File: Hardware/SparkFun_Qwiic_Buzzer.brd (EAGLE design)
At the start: 25.4 x 25.4 mm, 65 parts, among them J2 QWIIC_RA, J3 QWIIC_RA, Q3 200mA/40V, U4 ATTINY84-ARDUINO

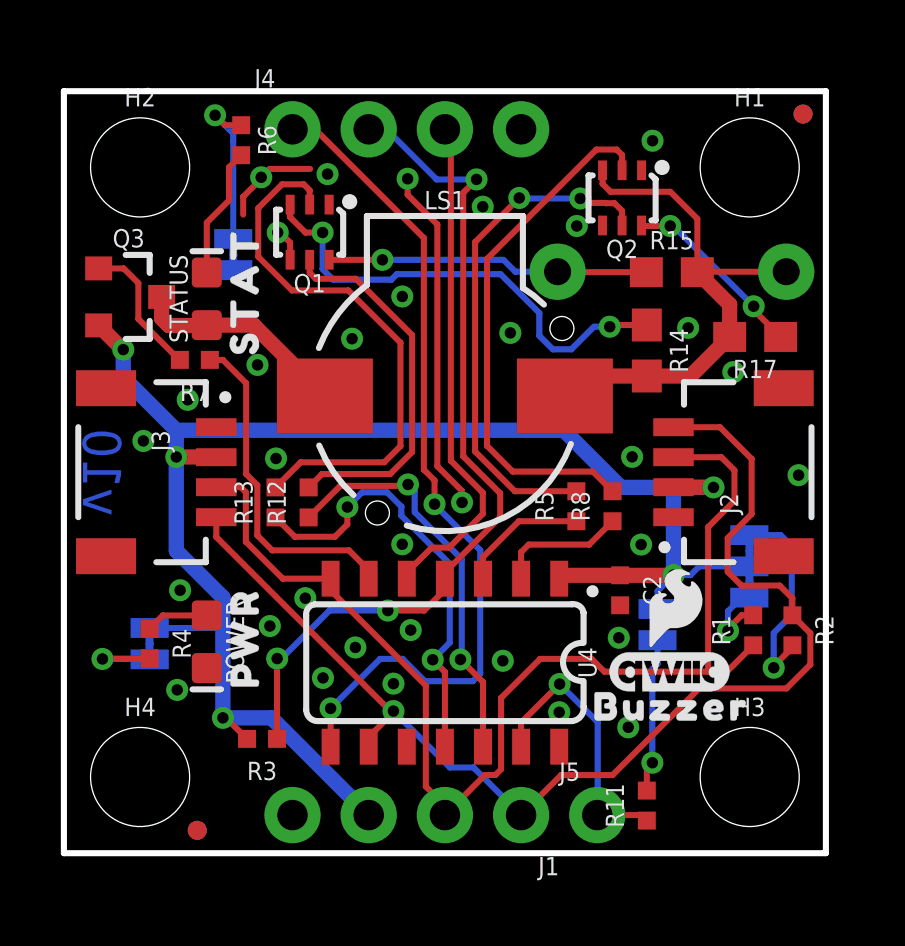
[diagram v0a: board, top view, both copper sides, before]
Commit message: group review pre-meeting
-add flyback diode
-add tPlace lines to divide tightly packed passives
-add 10uF cap on 3V3 rail
-corrected name on I2C Jumper
-Added JP1 to allow user to easily remove R15 resistor when using USER PTH resistor for volume control
-fixes some acid traps on poci and rst headers
-increased trace from USER resistor to BJT.
-trigger net renames to have active low in the name
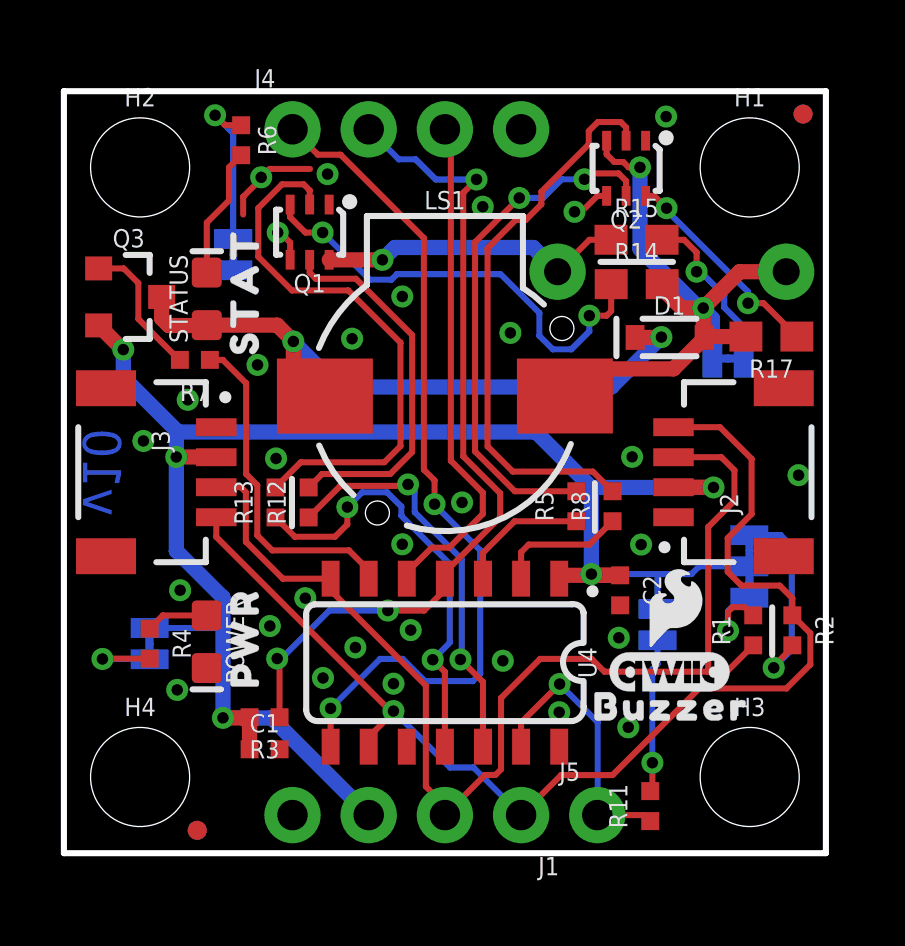
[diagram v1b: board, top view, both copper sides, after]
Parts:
- added C1: 10uF, SparkFun-Capacitors:0402-TIGHT
- added D1: 0.5A/40V/420mV, SparkFun-DiscreteSemi:SOD-323
- added JP1: (no value), SparkFun-Jumpers:SMT-JUMPER_2_NC_TRACE_SILK
- added U$5: (no value), output:#PWR_LED#13
- U$6: device output:#PWR#4 -> output:#JP1#14
- moved U$6 17.7 mm to (19.5, 16.3), turned to 0 degrees
- moved R14 2.24 mm to (19.1, 19.0), turned to 0 degrees
- moved R15 1.60 mm to (19.1, 20.4)
- moved Q2 0.99 mm to (18.7, 22.8)
- moved R3 0.73 mm to (6.69, 4.53)
- moved R17 0.54 mm to (23.6, 17.2)
- moved R11 0.12 mm to (19.5, 1.57)
- renumbered JP3 to I2C, PWR to PWR_LED
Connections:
- net TRIGGER renamed !TRIGGER!
- new net N$16: JP1.1, R15.2
- net 3.3V: now also C1.1
- net GND: now also C1.2
- net N$4: now also D1.A, JP1.2; no longer R15.2
- net N$6: now also D1.C
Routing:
- net N$6: track 7.24 -> 22.2 mm, vias 0 -> 2
- net GND: track 15.9 -> 5.67 mm, vias 33 -> 30
- net N$16: track 0.00 -> 5.59 mm, vias 0 -> 1
- net N$4: track 17.8 -> 22.1 mm, vias 0 -> 2
- net 3.3V: track 56.7 -> 59.2 mm
- net N$12: track 17.6 -> 18.8 mm
- net N$13: track 6.25 -> 7.25 mm
- net !RST: track 28.6 -> 28.0 mm
- net SDA_PU1: track 2.65 -> 3.21 mm
- net N$14: track 15.8 -> 15.3 mm

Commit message: reduced size of qwiic logo and buzzer test on bottom silk
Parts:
- removed U$14: (no value), output:BUZZER0
- added U$22: (no value), output:BUZZER14
- U$16: device SparkFun-Aesthetics:QWIIC_7MM -> SparkFun-Aesthetics:QWIIC_5MM
- moved U$16 0.49 mm to (13.1, 10.3)
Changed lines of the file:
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@@
 <drawing>
 <settings>
-<setting alwaysvectorfont="yes"/>
+<setting alwaysvectorfont="no"/>
 <setting keepoldvectorfont="yes"/>
 <setting verticaltext="up"/>
@@
 <grid distance="0.05" unitdist="inch" unit="inch" style="lines" multiple="1" display="yes" altdistance="0.0001" altunitdist="inch" altunit="inch"/>
 <layers>
-<layer number="1" name="Top" color="4" fill="1" visible="yes" active="yes"/>
-<layer number="16" name="Bottom" color="1" fill="1" visible="yes" active="yes"/>
+<layer number="1" name="Top" color="4" fill="1" visible="no" active="yes"/>
+<layer number="16" name="Bottom" color="1" fill="1" visible="no" active="yes"/>
 <layer number="17" name="Pads" color="2" fill="1" visible="yes" active="yes"/>
 <layer number="18" name="Vias" color="2" fill="1" visible="yes" active="yes"/>
-<layer number="19" name="Unrouted" color="6" fill="1" visible="yes" active="yes"/>
-<layer number="20" name="Dimension" color="24" fill="1" visible="yes" active="yes"/>
-<layer number="21" name="tPlace" color="16" fill="1" visible="yes" active="yes"/>
+<layer number="19" name="Unrouted" color="6" fill="1" visible="no" active="yes"/>
+<layer number="20" name="Dimension" color="24" fill="1" visible="no" active="yes"/>
+<layer number="21" name="tPlace" color="16" fill="1" visible="no" active="yes"/>
 <layer number="22" name="bPlace" color="14" fill="1" visible="yes" active="yes"/>
-<layer number="23" name="tOrigins" color="15" fill="1" visible="yes" active="yes"/>
+<layer number="23" name="tOrigins" color="15" fill="1" visible="no" active="yes"/>
 <layer number="24" name="bOrigins" color="15" fill="1" visible="yes" active="yes"/>
 <layer number="25" name="tNames" color="7" fill="1" visible="no" active="yes"/>
@@
 <layer number="37" name="tTest" color="7" fill="1" visible="no" active="yes"/>
 <layer number="38" name="bTest" color="7" fill="1" visible="no" active="yes"/>
-<layer number="39" name="tKeepout" color="4" fill="11" visible="yes" active="yes"/>
+<layer number="39" name="tKeepout" color="4" fill="11" visible="no" active="yes"/>
 <layer number="40" name="bKeepout" color="1" fill="11" visible="no" active="yes"/>
 <layer number="41" name="tRestrict" color="4" fill="10" visible="no" active="yes"/>
@@
 <layer number="43" name="vRestrict" color="2" fill="10" visible="no" active="yes"/>
 <layer number="44" name="Drills" color="7" fill="1" visible="no" active="yes"/>
-<layer number="45" name="Holes" color="7" fill="1" visible="yes" active="yes"/>
+<layer number="45" name="Holes" color="7" fill="1" visible="no" active="yes"/>
 <layer number="46" name="Milling" color="3" fill="1" visible="no" active="yes"/>
 <layer number="47" name="Measures" color="7" fill="1" visible="no" active="yes"/>
 <layer number="48" name="Document" color="7" fill="1" visible="no" active="yes"/>
-<layer number="49" name="Reference" color="7" fill="1" visible="yes" active="yes"/>
+<layer number="49" name="Reference" color="7" fill="1" visible="no" active="yes"/>
 <layer number="50" name="dxf" color="7" fill="1" visible="no" active="yes"/>
-<layer number="51" name="tDocu" color="6" fill="1" visible="yes" active="yes"/>
+<layer number="51" name="tDocu" color="6" fill="1" visible="no" active="yes"/>
 <layer number="52" name="bDocu" color="7" fill="1" visible="no" active="yes"/>
 <layer number="91" name="Nets" color="2" fill="1" visible="no" active="no"/>
@@
 <element name="U$9" library="output" package="PWR0" value="" x="6.0325" y="7.1755" smashed="yes" rot="R90"/>
 <element name="U$3" library="SparkFun-Aesthetics" package="QWIIC_4MM" value="" x="20.193" y="6.0325" smashed="yes"/>
-<element name="U$14" library="output" package="BUZZER0" value="" x="12.72031875" y="7.7851" smashed="yes" rot="MR0"/>
-<element name="U$16" library="SparkFun-Aesthetics" package="QWIIC_7MM" value="" x="12.827" y="9.906" smashed="yes" rot="MR0"/>
+<element name="U$16" library="SparkFun-Aesthetics" package="QWIIC_5MM" value="" x="13.1064" y="10.3124" smashed="yes" rot="MR0"/>
 <element name="U$13" library="output" package="BUZZER1" value="" x="20.2565" y="4.8895" smashed="yes"/>
 <element name="U$11" library="output" package="#I2C#0" value="" x="22.8574625" y="12.791440625" smashed="yes" rot="MR90"/>
@@
 <element name="U$5" library="output" package="#PWR_LED#13" value="" x="2.8448" y="12.1793" smashed="yes" rot="MR90"/>
 <element name="U$6" library="output" package="#JP1#14" value="" x="19.466559375" y="16.304259375" smashed="yes" rot="MR0"/>
+<element name="U$22" library="output" package="BUZZER14" value="" x="12.849859375" y="8.7985625" smashed="yes" rot="MR0"/>
 </elements>
 <signals>

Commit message: Corrected GND header silk label
-rotated GND header silk label to match others
-updated VCC note in sch to show typically 3.3V via QWIIC.
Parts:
- turned U$2 to 90 degrees
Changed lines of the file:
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@@
 <drawing>
 <settings>
-<setting alwaysvectorfont="no"/>
+<setting alwaysvectorfont="yes"/>
 <setting keepoldvectorfont="yes"/>
 <setting verticaltext="up"/>
@@
 <grid distance="0.05" unitdist="inch" unit="inch" style="lines" multiple="1" display="yes" altdistance="0.0001" altunitdist="inch" altunit="inch"/>
 <layers>
-<layer number="1" name="Top" color="4" fill="1" visible="no" active="yes"/>
-<layer number="16" name="Bottom" color="1" fill="1" visible="no" active="yes"/>
+<layer number="1" name="Top" color="4" fill="1" visible="yes" active="yes"/>
+<layer number="16" name="Bottom" color="1" fill="1" visible="yes" active="yes"/>
 <layer number="17" name="Pads" color="2" fill="1" visible="yes" active="yes"/>
 <layer number="18" name="Vias" color="2" fill="1" visible="yes" active="yes"/>
-<layer number="19" name="Unrouted" color="6" fill="1" visible="no" active="yes"/>
-<layer number="20" name="Dimension" color="24" fill="1" visible="no" active="yes"/>
-<layer number="21" name="tPlace" color="16" fill="1" visible="no" active="yes"/>
+<layer number="19" name="Unrouted" color="6" fill="1" visible="yes" active="yes"/>
+<layer number="20" name="Dimension" color="24" fill="1" visible="yes" active="yes"/>
+<layer number="21" name="tPlace" color="16" fill="1" visible="yes" active="yes"/>
 <layer number="22" name="bPlace" color="14" fill="1" visible="yes" active="yes"/>
-<layer number="23" name="tOrigins" color="15" fill="1" visible="no" active="yes"/>
+<layer number="23" name="tOrigins" color="15" fill="1" visible="yes" active="yes"/>
 <layer number="24" name="bOrigins" color="15" fill="1" visible="yes" active="yes"/>
 <layer number="25" name="tNames" color="7" fill="1" visible="no" active="yes"/>
@@
 <layer number="43" name="vRestrict" color="2" fill="10" visible="no" active="yes"/>
 <layer number="44" name="Drills" color="7" fill="1" visible="no" active="yes"/>
-<layer number="45" name="Holes" color="7" fill="1" visible="no" active="yes"/>
+<layer number="45" name="Holes" color="7" fill="1" visible="yes" active="yes"/>
 <layer number="46" name="Milling" color="3" fill="1" visible="no" active="yes"/>
 <layer number="47" name="Measures" color="7" fill="1" visible="no" active="yes"/>
 <layer number="48" name="Document" color="7" fill="1" visible="no" active="yes"/>
-<layer number="49" name="Reference" color="7" fill="1" visible="no" active="yes"/>
+<layer number="49" name="Reference" color="7" fill="1" visible="yes" active="yes"/>
 <layer number="50" name="dxf" color="7" fill="1" visible="no" active="yes"/>
-<layer number="51" name="tDocu" color="6" fill="1" visible="no" active="yes"/>
+<layer number="51" name="tDocu" color="6" fill="1" visible="yes" active="yes"/>
 <layer number="52" name="bDocu" color="7" fill="1" visible="no" active="yes"/>
 <layer number="91" name="Nets" color="2" fill="1" visible="no" active="no"/>
@@
 <element name="U$13" library="output" package="BUZZER1" value="" x="20.2565" y="4.8895" smashed="yes"/>
 <element name="U$11" library="output" package="#I2C#0" value="" x="22.8574625" y="12.791440625" smashed="yes" rot="MR90"/>
-<element name="U$2" library="output" package="#GND#0" value="" x="7.62" y="4.0005" smashed="yes" rot="MR270"/>
+<element name="U$2" library="output" package="#GND#0" value="" x="7.5946" y="4.005578125" smashed="yes" rot="MR90"/>
 <element name="U$10" library="output" package="#GND#0" value="" x="17.78" y="24.13" smashed="yes" rot="MR0"/>
 <element name="U$17" library="output" package="#3V3#0" value="" x="10.0965" y="4.0005" smashed="yes" rot="MR90"/>

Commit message: post review tweaks
-removed INT pin feature (both header pin and pullup resistor)
-changed TRIGGER pin to use POCI pin. It will be there for programming as needed, but this naming omits any mention of SPI, making it really clear this doesn't do SPI.
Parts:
- removed INT: JUMPER-SMT_2_NC_TRACE_SILK, SparkFun-Jumpers:SMT-JUMPER_2_NC_TRACE_SILK
- removed J4: (no value), SparkFun-Connectors:1X04_NO_SILK
- removed J5: (no value), SparkFun-Connectors:1X01_NO_SILK
- removed R11: 10k, SparkFun-Resistors:0402-TIGHT
- removed U$20: (no value), output:##INT##0
- removed U$21: (no value), output:#INT#10
- removed U$4: (no value), output:#POCI#11
- added J6: (no value), SparkFun-Connectors:1X03_NO_SILK
- moved LOGO1 21.8 mm to (20.2, 5.99)
- moved U$10 4.58 mm to (14.0, 21.6), turned to 90 degrees
- moved U$12 1.28 mm to (8.89, 21.7)
- moved J1 1.27 mm to (16.5, 1.27)
- moved U$19 1.27 mm to (14.0, 4.00)
- moved U$15 1.27 mm to (11.4, 21.3)
- moved U$17 1.27 mm to (11.4, 4.00)
- moved U$18 1.27 mm to (16.6, 3.87)
- moved U$2 1.27 mm to (8.86, 4.01)
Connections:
- removed net !INT: J5.1, R11.1, U4.13
- removed net INT_R: INT.1, R11.2
- removed net POCI: J4.1, U4.8
- net !RST: now also J6.1; no longer J4.2
- net !TRIGGER!: now also J6.2, U4.8; no longer J4.3, U4.5
- net 3.3V: no longer INT.2
- net GND: now also J6.3; no longer J4.4
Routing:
- net POCI: track 28.5 -> 0.00 mm, vias 2 -> 0
- net !TRIGGER!: track 16.9 -> 28.5 mm, vias 0 -> 2
- net !INT: track 9.37 -> 0.00 mm, vias 1 -> 0
- net INT_R: track 5.13 -> 0.00 mm, vias 1 -> 0
- net SDA: track 39.2 -> 38.2 mm
- net !RST: track 28.0 -> 28.9 mm
- net N$14: track 15.3 -> 16.1 mm
- net GND: vias 30 -> 29

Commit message: finalized resistor values on vol control
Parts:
- R12, R13, R5, R7, R8: value 100 -> 330
- R14, R15: device SparkFun-Resistors:0603 -> SparkFun-Resistors:0402-TIGHT
- R17: value 1k -> 2.2k; device SparkFun-Resistors:0603 -> SparkFun-Resistors:0402-TIGHT
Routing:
- net N$4: track 22.1 -> 22.7 mm
